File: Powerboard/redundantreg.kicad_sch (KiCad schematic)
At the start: 34 parts, among them Q10 MCH6351, Q9 MCH6351, U6 LM2679T-3.3-iclr, U7 LM2679T-3.3-iclr, U8 LTC4412xS6, U9 LTC4412xS6

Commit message: assigned FPs for ceramic caps & most resistors
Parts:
- C36, C37, C48, C49: footprint (none) -> Capacitor_SMD:C_0603_1608Metric
- C42, C43: footprint (none) -> Capacitor_SMD:C_0805_2012Metric
- D5, D6: footprint DPAK229P990X238-3N -> (none)
- L3, L4: footprint P0846SNL -> (none)
- U6, U7: footprint TO127P457X1016X2052-7P -> (none)
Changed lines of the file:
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@@
       (effects (font (size 1.27 1.27)) (justify left))
     )
-    (property "Footprint" "" (id 2) (at 69.85 149.86 0)
+    (property "Footprint" "Capacitor_SMD:C_0805_2012Metric" (id 2) (at 69.85 149.86 0)
       (effects (font (size 1.27 1.27)) hide)
     )
@@
       (effects (font (size 1.27 1.27)) (justify left))
     )
-    (property "Footprint" "" (id 2) (at 68.58 27.94 0)
+    (property "Footprint" "Capacitor_SMD:C_0805_2012Metric" (id 2) (at 68.58 27.94 0)
       (effects (font (size 1.27 1.27)) hide)
     )
@@
     (property "Reference" "C48" (id 0) (at 168.91 125.095 90))
     (property "Value" "0.1µF" (id 1) (at 168.91 127.4064 90))
-    (property "Footprint" "" (id 2) (at 168.91 130.81 0)
+    (property "Footprint" "Capacitor_SMD:C_0603_1608Metric" (id 2) (at 168.91 130.81 0)
       (effects (font (size 1.27 1.27)) hide)
     )
@@
     (property "Reference" "C49" (id 0) (at 186.69 38.735 90))
     (property "Value" "0.1µF" (id 1) (at 186.69 41.0464 90))
-    (property "Footprint" "" (id 2) (at 186.69 44.45 0)
+    (property "Footprint" "Capacitor_SMD:C_0603_1608Metric" (id 2) (at 186.69 44.45 0)
       (effects (font (size 1.27 1.27)) hide)
     )
@@
     (property "Reference" "U6" (id 0) (at 102.87 16.002 0))
     (property "Value" "LM2679T-3.3-iclr" (id 1) (at 102.87 18.3134 0))
-    (property "Footprint" "TO127P457X1016X2052-7P" (id 2) (at 102.87 25.4 0)
+    (property "Footprint" "" (id 2) (at 102.87 25.4 0)
       (effects (font (size 1.27 1.27)) (justify left bottom) hide)
     )
@@
     (property "Reference" "U7" (id 0) (at 104.14 137.922 0))
     (property "Value" "LM2679T-3.3-iclr" (id 1) (at 104.14 140.2334 0))
-    (property "Footprint" "TO127P457X1016X2052-7P" (id 2) (at 104.14 147.32 0)
+    (property "Footprint" "" (id 2) (at 104.14 147.32 0)
       (effects (font (size 1.27 1.27)) (justify left bottom) hide)
     )
@@
     (property "Reference" "L4" (id 0) (at 146.05 141.605 0))
     (property "Value" "15uH" (id 1) (at 146.05 143.9164 0))
-    (property "Footprint" "P0846SNL" (id 2) (at 152.4 146.05 0)
+    (property "Footprint" "" (id 2) (at 152.4 146.05 0)
       (effects (font (size 1.27 1.27)) (justify left) hide)
     )
@@
       (effects (font (size 1.27 1.27)) (justify right))
     )
-    (property "Footprint" "DPAK229P990X238-3N" (id 2) (at 134.62 158.75 0)
+    (property "Footprint" "" (id 2) (at 134.62 158.75 0)
       (effects (font (size 1.27 1.27)) (justify left bottom) hide)
     )
@@
     (property "Reference" "L3" (id 0) (at 144.78 19.685 0))
     (property "Value" "15uH" (id 1) (at 144.78 21.9964 0))
-    (property "Footprint" "P0846SNL" (id 2) (at 151.13 24.13 0)
+    (property "Footprint" "" (id 2) (at 151.13 24.13 0)
       (effects (font (size 1.27 1.27)) (justify left) hide)
     )
@@
       (effects (font (size 1.27 1.27)) (justify right))
     )
-    (property "Footprint" "DPAK229P990X238-3N" (id 2) (at 133.35 36.83 0)
+    (property "Footprint" "" (id 2) (at 133.35 36.83 0)
       (effects (font (size 1.27 1.27)) (justify left bottom) hide)
     )
@@
     (property "Reference" "C37" (id 0) (at 104.1463 131.8981 90))
     (property "Value" "0.01uF" (id 1) (at 104.1463 134.435 90))
-    (property "Footprint" "" (id 2) (at 104.14 137.16 0)
+    (property "Footprint" "Capacitor_SMD:C_0603_1608Metric" (id 2) (at 104.14 137.16 0)
       (effects (font (size 1.27 1.27)) hide)
     )
@@
     (property "Reference" "C36" (id 0) (at 102.8763 7.4381 90))
     (property "Value" "0.01uF" (id 1) (at 102.8763 9.975 90))
-    (property "Footprint" "" (id 2) (at 102.87 12.7 0)
-      (effects (font (size 1.27 1.27)) hide)
-    )
+    (property "Footprint" "Capacitor_SMD:C_0603_1608Metric" (id 2) (at 102.87 12.7 0)
+      (effects (font (size 1.27 1.27)) hide)
+    )

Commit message: actually changed caps this time
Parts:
- C48, C49: footprint Capacitor_SMD:C_0603_1608Metric -> (none)
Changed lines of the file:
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@@
     (property "Reference" "C48" (id 0) (at 168.91 125.095 90))
     (property "Value" "0.1µF" (id 1) (at 168.91 127.4064 90))
-    (property "Footprint" "Capacitor_SMD:C_0603_1608Metric" (id 2) (at 168.91 130.81 0)
+    (property "Footprint" "" (id 2) (at 168.91 130.81 0)
       (effects (font (size 1.27 1.27)) hide)
     )
@@
     (property "Reference" "C49" (id 0) (at 186.69 38.735 90))
     (property "Value" "0.1µF" (id 1) (at 186.69 41.0464 90))
-    (property "Footprint" "Capacitor_SMD:C_0603_1608Metric" (id 2) (at 186.69 44.45 0)
+    (property "Footprint" "" (id 2) (at 186.69 44.45 0)
       (effects (font (size 1.27 1.27)) hide)
     )

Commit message: All capacitors selected, most other footprints assigned
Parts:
- C19, C20, C29, C30, C34, C35: footprint (none) -> Capacitor_SMD:CP_Elec_5x5.3
- C38, C39, C40, C41, C44, C45, C46, C47: footprint (none) -> Capacitor_SMD:CP_Elec_10x10
- C48, C49: footprint (none) -> Capacitor_SMD:C_0603_1608Metric
- Q10, Q9: footprint (none) -> Package_TO_SOT_SMD:SOT-363_SC-70-6
- U6, U7: footprint (none) -> iclr:TO127P457X1016X2052-7P
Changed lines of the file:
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@@
     (property "Reference" "C48" (id 0) (at 168.91 125.095 90))
     (property "Value" "0.1µF" (id 1) (at 168.91 127.4064 90))
-    (property "Footprint" "" (id 2) (at 168.91 130.81 0)
+    (property "Footprint" "Capacitor_SMD:C_0603_1608Metric" (id 2) (at 168.91 130.81 0)
       (effects (font (size 1.27 1.27)) hide)
     )
@@
     (property "Reference" "C49" (id 0) (at 186.69 38.735 90))
     (property "Value" "0.1µF" (id 1) (at 186.69 41.0464 90))
-    (property "Footprint" "" (id 2) (at 186.69 44.45 0)
+    (property "Footprint" "Capacitor_SMD:C_0603_1608Metric" (id 2) (at 186.69 44.45 0)
       (effects (font (size 1.27 1.27)) hide)
     )
@@
     (property "Reference" "U6" (id 0) (at 102.87 16.002 0))
     (property "Value" "LM2679T-3.3-iclr" (id 1) (at 102.87 18.3134 0))
-    (property "Footprint" "" (id 2) (at 102.87 25.4 0)
+    (property "Footprint" "iclr:TO127P457X1016X2052-7P" (id 2) (at 102.87 25.4 0)
       (effects (font (size 1.27 1.27)) (justify left bottom) hide)
     )
@@
     (property "Reference" "U7" (id 0) (at 104.14 137.922 0))
     (property "Value" "LM2679T-3.3-iclr" (id 1) (at 104.14 140.2334 0))
-    (property "Footprint" "" (id 2) (at 104.14 147.32 0)
+    (property "Footprint" "iclr:TO127P457X1016X2052-7P" (id 2) (at 104.14 147.32 0)
       (effects (font (size 1.27 1.27)) (justify left bottom) hide)
     )
@@
       (effects (font (size 1.27 1.27)) (justify left))
     )
-    (property "Footprint" "" (id 2) (at 58.1152 158.75 0)
+    (property "Footprint" "Capacitor_SMD:CP_Elec_5x5.3" (id 2) (at 58.1152 158.75 0)
       (effects (font (size 1.27 1.27)) hide)
     )
@@
       (effects (font (size 1.27 1.27)) (justify left))
     )
-    (property "Footprint" "" (id 2) (at 44.1452 38.1 0)
+    (property "Footprint" "Capacitor_SMD:CP_Elec_5x5.3" (id 2) (at 44.1452 38.1 0)
       (effects (font (size 1.27 1.27)) hide)
     )
@@
       (effects (font (size 1.27 1.27)) (justify left))
     )
-    (property "Footprint" "" (id 2) (at 64.4652 158.75 0)
+    (property "Footprint" "Capacitor_SMD:CP_Elec_5x5.3" (id 2) (at 64.4652 158.75 0)
       (effects (font (size 1.27 1.27)) hide)
     )
@@
       (effects (font (size 1.27 1.27)) (justify left))
     )
-    (property "Footprint" "" (id 2) (at 171.1452 161.29 0)
+    (property "Footprint" "Capacitor_SMD:CP_Elec_10x10" (id 2) (at 171.1452 161.29 0)
       (effects (font (size 1.27 1.27)) hide)
     )
@@
       (effects (font (size 1.27 1.27)) (justify left))
     )
-    (property "Footprint" "" (id 2) (at 54.3052 38.1 0)
+    (property "Footprint" "Capacitor_SMD:CP_Elec_5x5.3" (id 2) (at 54.3052 38.1 0)
       (effects (font (size 1.27 1.27)) hide)
     )
@@
       (effects (font (size 1.27 1.27)) (justify left))
     )
-    (property "Footprint" "" (id 2) (at 154.6352 39.37 0)
+    (property "Footprint" "Capacitor_SMD:CP_Elec_10x10" (id 2) (at 154.6352 39.37 0)
       (effects (font (size 1.27 1.27)) hide)
     )
@@
     (property "Reference" "Q9" (id 0) (at 217.17 38.1 90))
     (property "Value" "MCH6351" (id 1) (at 217.17 40.64 90))
-    (property "Footprint" "" (id 2) (at 218.44 38.1 0)
+    (property "Footprint" "Package_TO_SOT_SMD:SOT-363_SC-70-6" (id 2) (at 218.44 38.1 0)
       (effects (font (size 1.27 1.27)) hide)
     )
@@
       (effects (font (size 1.27 1.27)) (justify left))
     )
-    (property "Footprint" "" (id 2) (at 166.0652 161.29 0)
+    (property "Footprint" "Capacitor_SMD:CP_Elec_10x10" (id 2) (at 166.0652 161.29 0)
       (effects (font (size 1.27 1.27)) hide)
     )
@@
       (effects (font (size 1.27 1.27)) (justify left))
     )
-    (property "Footprint" "" (id 2) (at 149.5552 39.37 0)
+    (property "Footprint" "Capacitor_SMD:CP_Elec_10x10" (id 2) (at 149.5552 39.37 0)
       (effects (font (size 1.27 1.27)) hide)
     )
@@
       (effects (font (size 1.27 1.27)) (justify left))
     )
-    (property "Footprint" "" (id 2) (at 159.7152 39.37 0)
+    (property "Footprint" "Capacitor_SMD:CP_Elec_10x10" (id 2) (at 159.7152 39.37 0)
       (effects (font (size 1.27 1.27)) hide)
     )
@@
     (property "Reference" "Q10" (id 0) (at 222.25 151.13 90))
     (property "Value" "MCH6351" (id 1) (at 222.25 153.67 90))
-    (property "Footprint" "" (id 2) (at 223.52 151.13 0)
+    (property "Footprint" "Package_TO_SOT_SMD:SOT-363_SC-70-6" (id 2) (at 223.52 151.13 0)
       (effects (font (size 1.27 1.27)) hide)
     )
@@
       (effects (font (size 1.27 1.27)) (justify left))
     )
-    (property "Footprint" "" (id 2) (at 160.9852 161.29 0)
+    (property "Footprint" "Capacitor_SMD:CP_Elec_10x10" (id 2) (at 160.9852 161.29 0)
       (effects (font (size 1.27 1.27)) hide)
     )
@@
       (effects (font (size 1.27 1.27)) (justify left))
     )
-    (property "Footprint" "" (id 2) (at 166.0652 39.37 0)
+    (property "Footprint" "Capacitor_SMD:CP_Elec_10x10" (id 2) (at 166.0652 39.37 0)
       (effects (font (size 1.27 1.27)) hide)
     )
@@
       (effects (font (size 1.27 1.27)) (justify left))
     )
-    (property "Footprint" "" (id 2) (at 60.6552 38.1 0)
+    (property "Footprint" "Capacitor_SMD:CP_Elec_5x5.3" (id 2) (at 60.6552 38.1 0)
       (effects (font (size 1.27 1.27)) hide)
     )
@@
       (effects (font (size 1.27 1.27)) (justify left))
     )
-    (property "Footprint" "" (id 2) (at 177.4952 161.29 0)
+    (property "Footprint" "Capacitor_SMD:CP_Elec_10x10" (id 2) (at 177.4952 161.29 0)
       (effects (font (size 1.27 1.27)) hide)
     )
@@
       (effects (font (size 1.27 1.27)) (justify left))
     )
-    (property "Footprint" "" (id 2) (at 47.9552 158.75 0)
-      (effects (font (size 1.27 1.27)) hide)
-    )
+    (property "Footprint" "Capacitor_SMD:CP_Elec_5x5.3" (id 2) (at 47.9552 158.75 0)
+      (effects (font (size 1.27 1.27)) hide)
+    )

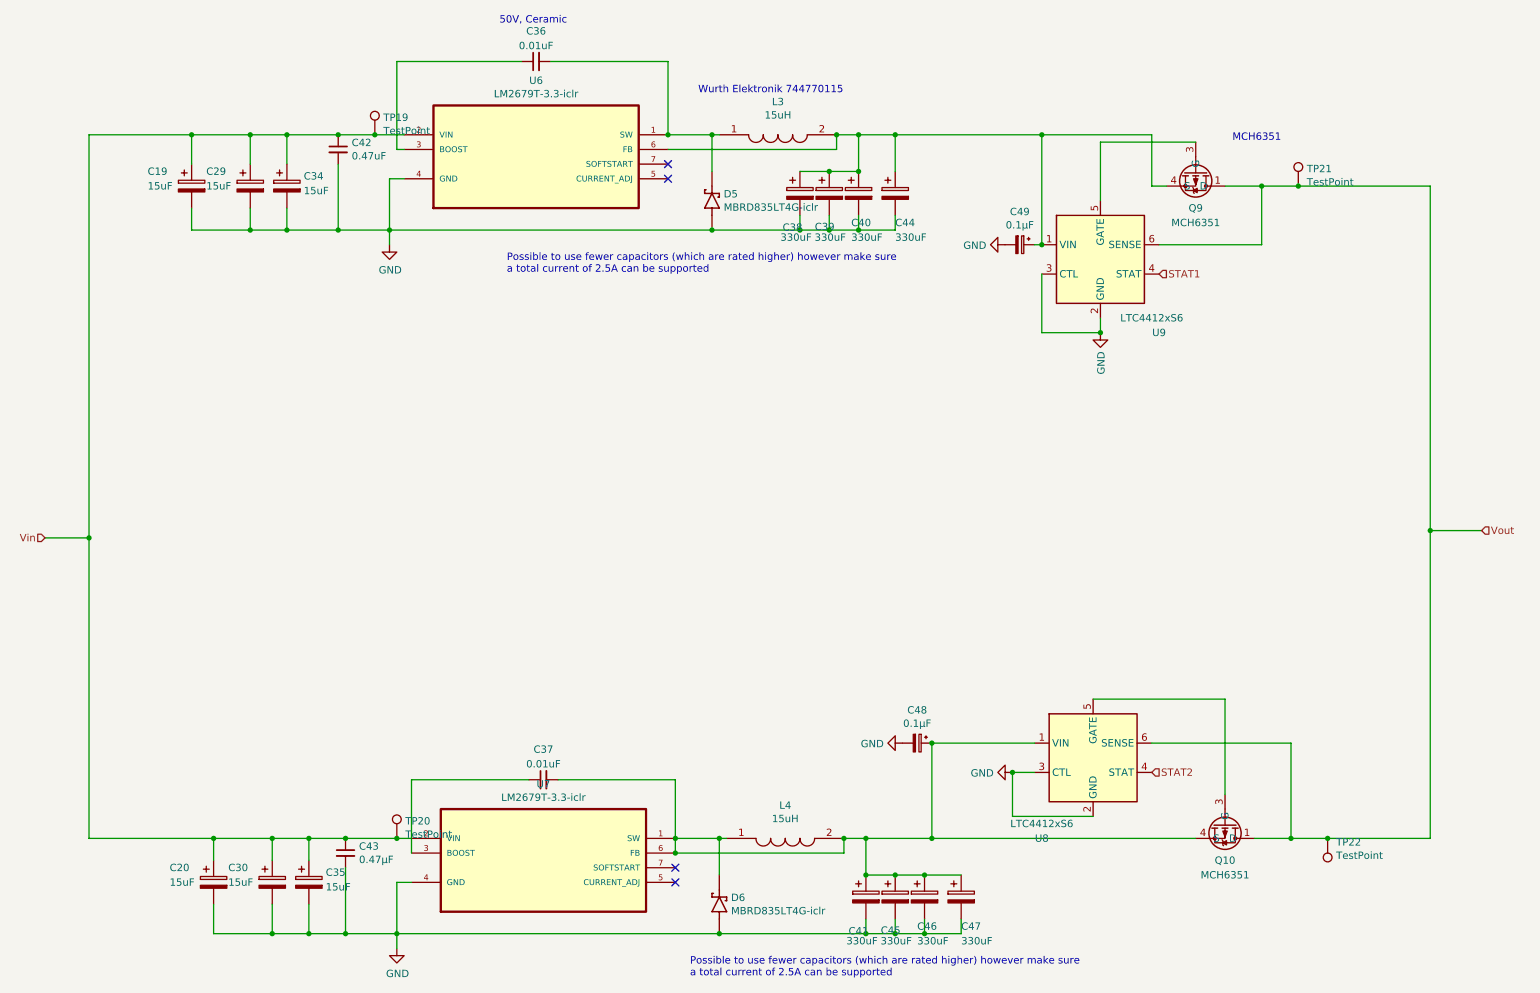
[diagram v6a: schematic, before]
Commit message: Finished footprint assignment
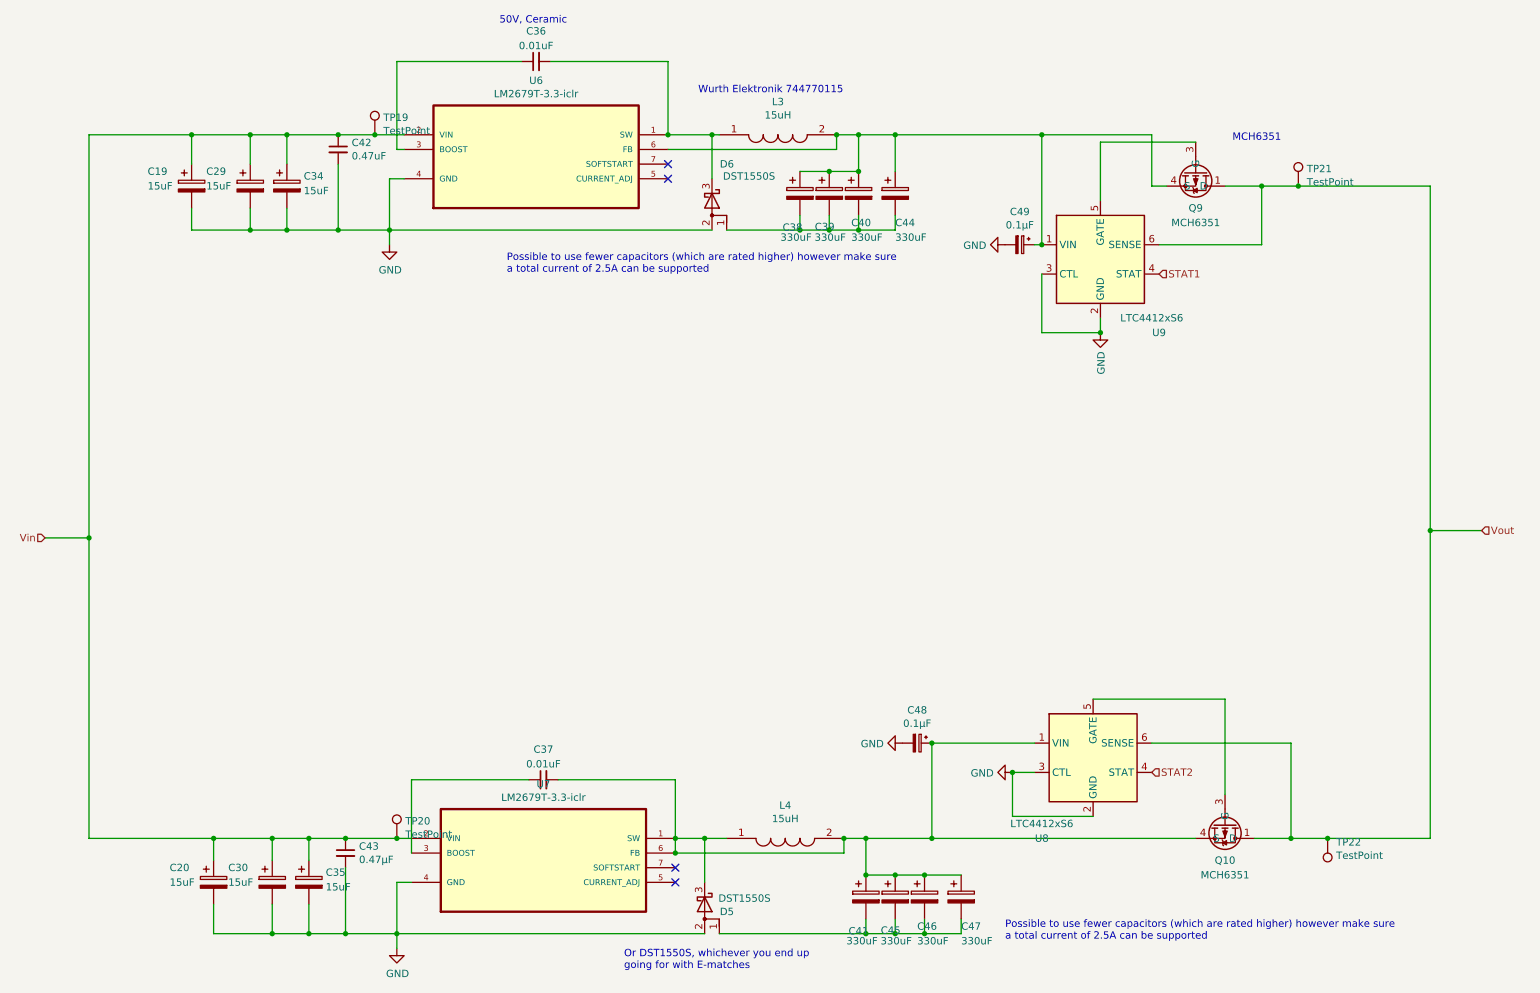
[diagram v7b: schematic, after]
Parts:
- removed D5, D6: MBRD835LT4G-iclr, symbol iclr:MBRD835LT4G-iclr
- added D5, D6: DST1550S, Package_TO_SOT_SMD:TO-277B, symbol Device:D_Schottky_AAK
- L3, L4: footprint (none) -> Inductor_SMD:L_12x12mm_H8mm
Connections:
- net GND: now also D5.2 (A), D6.2 (A); no longer C38.2, C39.2, C40.2, C41.2, C44.2, C45.2, C46.2, C47.2
- net at C37.2, C41.1, C45.1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: now also D5.3 (K)
- net at C36.2, L3.1, U6.1 (SW): now also D6.3 (K)
- new net: C41.2, C45.2, C46.2, C47.2, D5.1 (A)
- new net: C38.2, C39.2, C40.2, C44.2, D6.1 (A)
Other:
- note added: "Or DST1550S, whichever you end up going for with E-matches"

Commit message: changed some FP assignments and imported components
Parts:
- U6, U7: footprint iclr:TO127P457X1016X2052-7P -> Package_TO_SOT_SMD:TO-263-7_TabPin4
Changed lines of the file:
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@@
     (property "Reference" "U6" (id 0) (at 102.87 16.002 0))
     (property "Value" "LM2679T-3.3-iclr" (id 1) (at 102.87 18.3134 0))
-    (property "Footprint" "iclr:TO127P457X1016X2052-7P" (id 2) (at 102.87 25.4 0)
+    (property "Footprint" "Package_TO_SOT_SMD:TO-263-7_TabPin4" (id 2) (at 102.87 25.4 0)
       (effects (font (size 1.27 1.27)) (justify left bottom) hide)
     )
@@
     (property "Reference" "U7" (id 0) (at 104.14 137.922 0))
     (property "Value" "LM2679T-3.3-iclr" (id 1) (at 104.14 140.2334 0))
-    (property "Footprint" "iclr:TO127P457X1016X2052-7P" (id 2) (at 104.14 147.32 0)
+    (property "Footprint" "Package_TO_SOT_SMD:TO-263-7_TabPin4" (id 2) (at 104.14 147.32 0)
       (effects (font (size 1.27 1.27)) (justify left bottom) hide)
     )
